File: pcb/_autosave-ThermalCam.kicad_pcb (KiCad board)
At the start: 2 copper layers, 127 x 37 mm, 39 parts, among them J1 USB_B_Mini, SW2 SW_Push, SW3 SW_Push, U1 AMS1117-3.3, U2 AMG8833, U4 ESP32-WROOM-32, U5 ILI9341-HLG-18, U6 Arducam_SPI, U7 ESP32_PROG

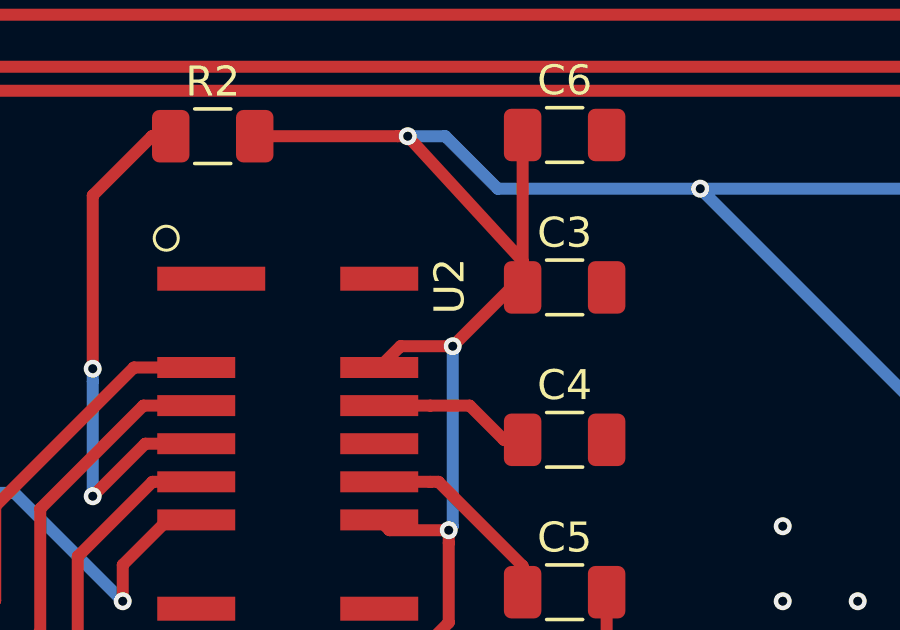
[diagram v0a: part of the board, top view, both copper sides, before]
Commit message: added eastrising 1.44 tft
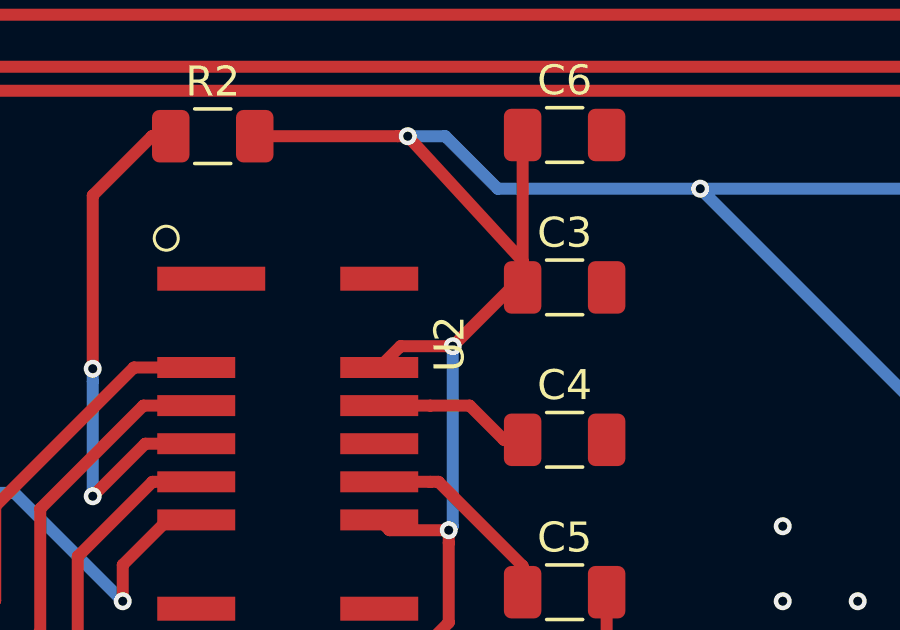
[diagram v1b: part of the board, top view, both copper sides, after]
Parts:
- C11: value 10uf -> 100nf
- C2: value 100uf -> 100nf
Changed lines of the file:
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@@
   )
   (setup
-    (last_trace_width 0.2)
+    (last_trace_width 0.4)
     (user_trace_width 0.2)
     (user_trace_width 0.4)
@@
     (visible_elements 7FFFFFFF)
     (pcbplotparams
-      (layerselection 0x010f0_ffffffff)
+      (layerselection 0x01000_7fffffff)
       (usegerberextensions false)
       (usegerberattributes false)
@@
       (drillshape 0)
       (scaleselection 1)
-      (outputdirectory "C:/Users/rwrif/Desktop/jclpcb/"))
+      (outputdirectory "C:/Users/rwrif/Desktop/cnc"))
   )
   (net 0 "")
@@
     (add_net "Net-(D1-Pad1)")
     (add_net "Net-(D2-Pad1)")
+    (add_net "Net-(J1-Pad2)")
+    (add_net "Net-(J1-Pad3)")
+    (add_net "Net-(J1-Pad4)")
     (add_net "Net-(R1-Pad2)")
     (add_net "Net-(R11-Pad1)")
     (add_net "Net-(R12-Pad1)")
     (add_net "Net-(R2-Pad1)")
+    (add_net "Net-(U4-Pad14)")
+    (add_net "Net-(U4-Pad17)")
+    (add_net "Net-(U4-Pad18)")
+    (add_net "Net-(U4-Pad19)")
+    (add_net "Net-(U4-Pad20)")
+    (add_net "Net-(U4-Pad27)")
+    (add_net "Net-(U4-Pad28)")
+    (add_net "Net-(U4-Pad32)")
+    (add_net "Net-(U4-Pad33)")
+    (add_net "Net-(U4-Pad36)")
+    (add_net "Net-(U4-Pad4)")
+    (add_net "Net-(U4-Pad5)")
+    (add_net "Net-(U4-Pad6)")
+    (add_net "Net-(U4-Pad7)")
+    (add_net "Net-(U4-Pad8)")
+    (add_net "Net-(U4-Pad9)")
     (add_net RESET_TFT)
     (add_net SCL)
@@
   (module AMG8833:XDCR_AMG8833 (layer F.Cu)
     (at 168.5 37.25 270)
-    (fp_text reference U2 (at -5.25 -5.393685 90) (layer F.SilkS)
-      (effects (font (size 1.001614 1.001614) (thickness 0.15)))
+    (fp_text reference U2 (at -3.330345 -5.393685 90) (layer F.SilkS)
+      (effects (font (size 1.001614 1.001614) (thickness 0.015)))
     )
     (fp_text value AMG8833 (at 1.12305 5.63009 90) (layer F.Fab)
@@
       (effects (font (size 1 1) (thickness 0.15)))
     )
-    (fp_text value 10uf (at 0 1.82) (layer F.Fab)
+    (fp_text value 100nf (at 0 1.82) (layer F.Fab)
       (effects (font (size 1 1) (thickness 0.15)))
     )
@@
       (effects (font (size 1 1) (thickness 0.15)))
     )
-    (fp_text value 100uf (at 0 1.82) (layer F.Fab)
-      (effects (font (size 1 1) (thickness 0.15)))
-    )
+    (fp_text value 100nf (at 0 1.82) (layer F.Fab)
+      (effects (font (size 1 1) (thickness 0.15)))
+    )
